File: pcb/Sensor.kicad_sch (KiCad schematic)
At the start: 38 parts, among them IC2 74HC14D-Q100,118, U5 OPA2376xxD

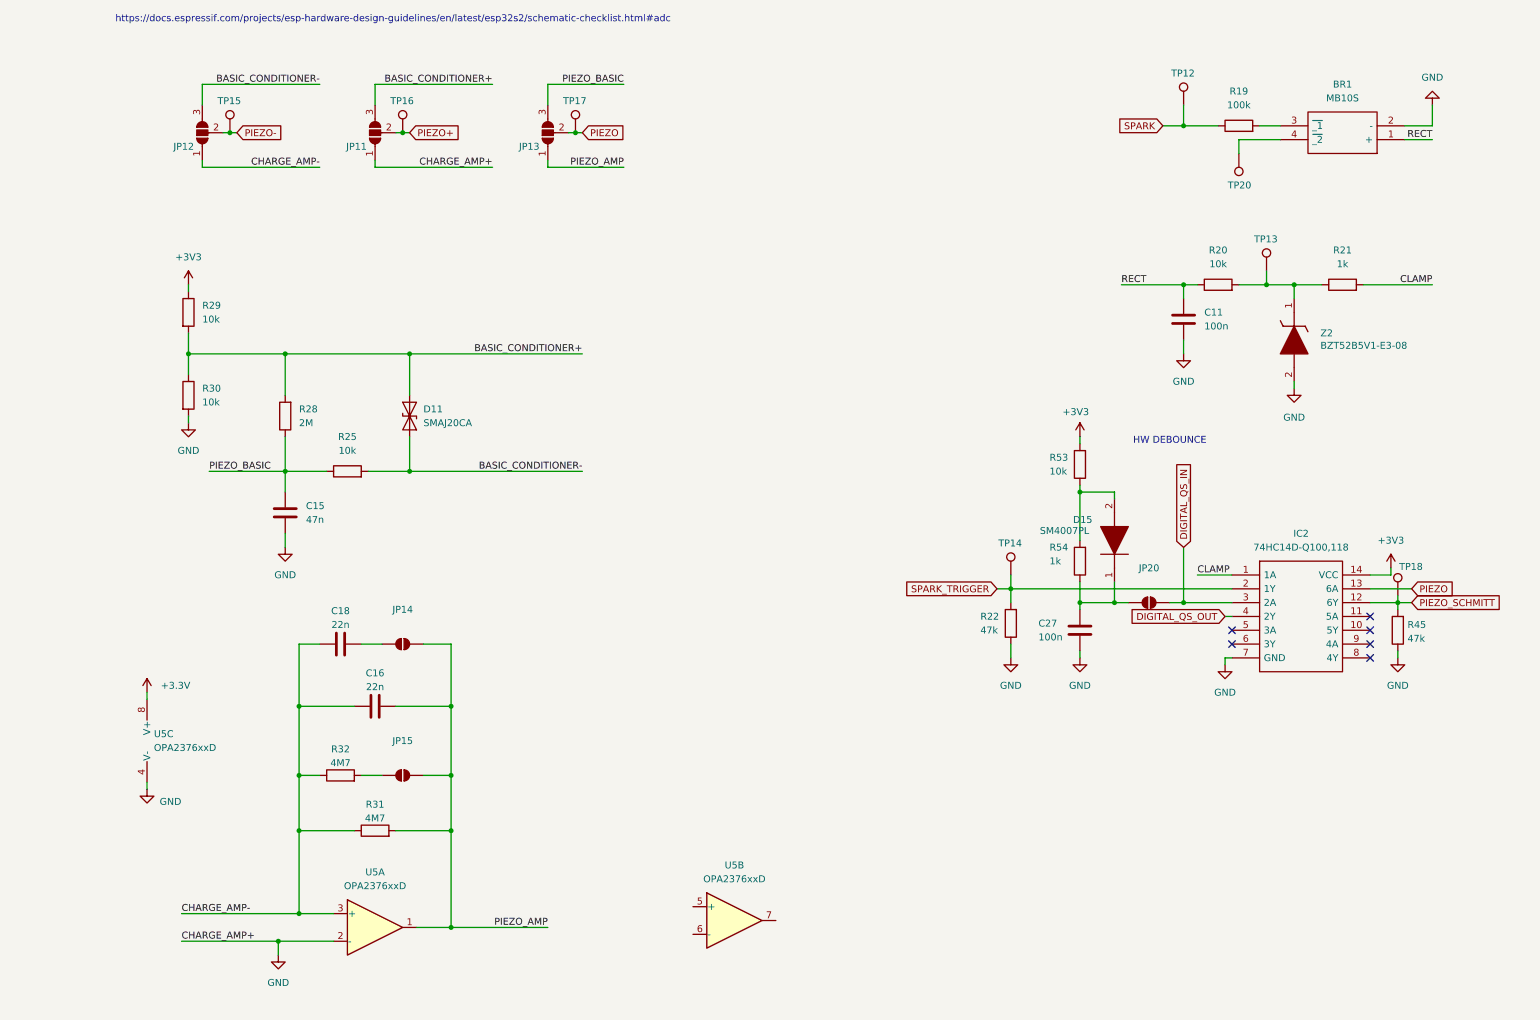
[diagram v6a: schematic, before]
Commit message: enhanced spark detection circuit
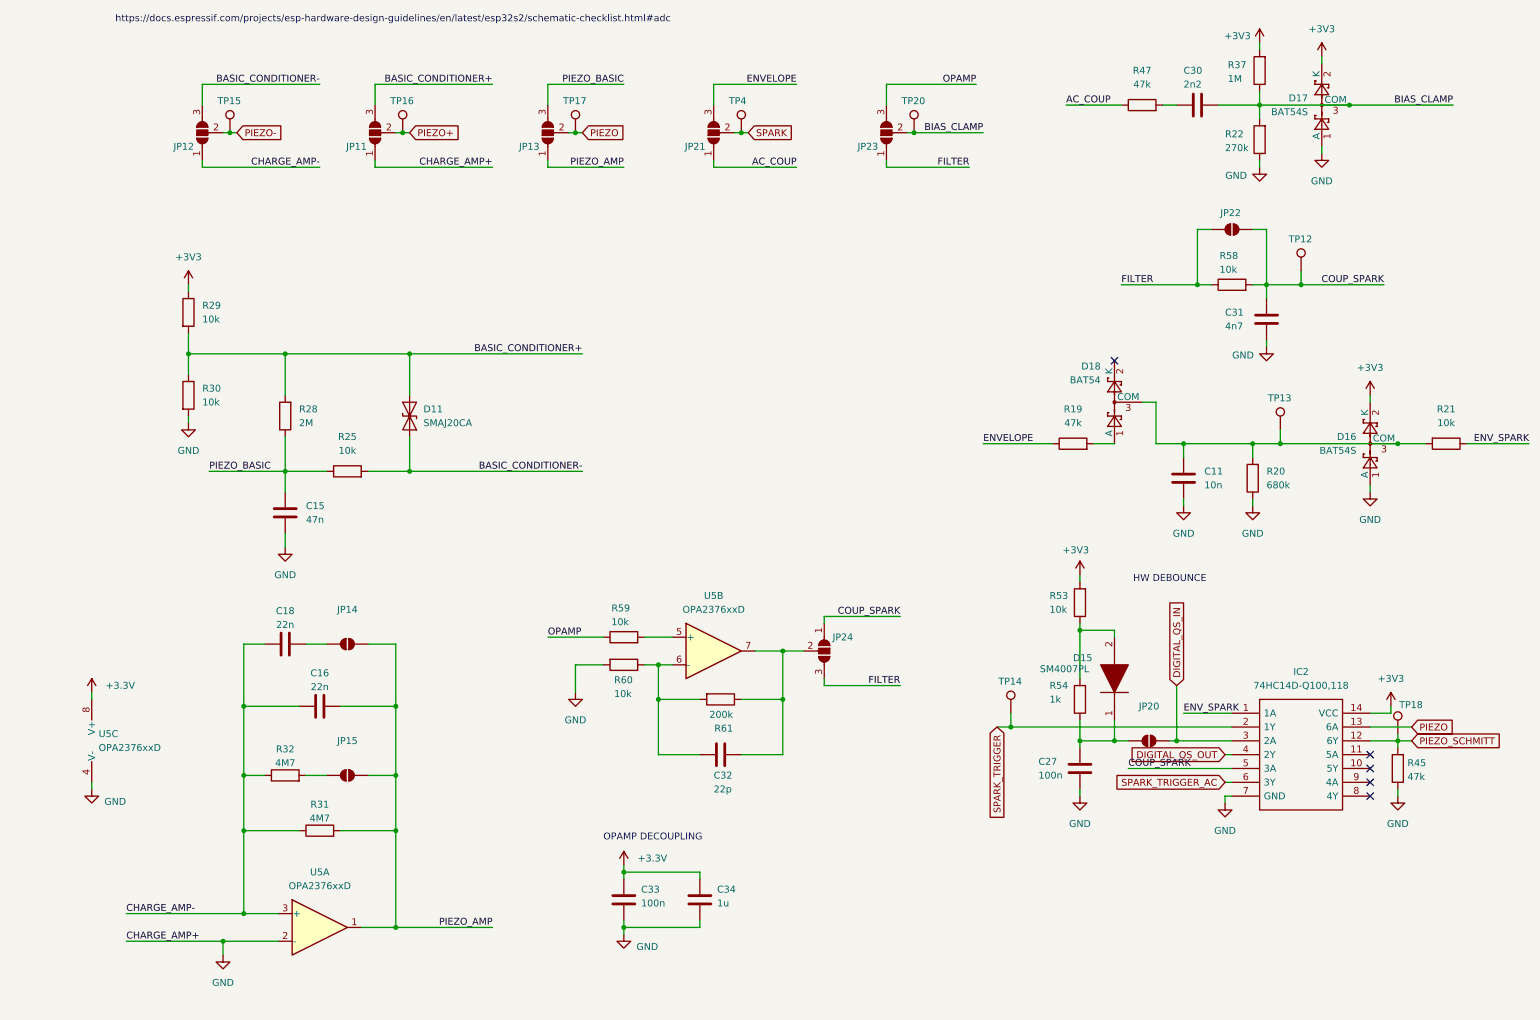
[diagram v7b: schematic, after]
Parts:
- removed BR1: MB10S, SamacSys_Parts:SOP245P670X290-4N, symbol SamacSys_Parts:MB10S
- removed Z2: BZT52B5V1-E3-08, SamacSys_Parts:BZT52B5V1E308, symbol SamacSys_Parts:BZT52B5V1-E3-08
- added C30: 2n2, Capacitor_SMD:C_0603_1608Metric, symbol Device:C
- added C31: 4n7, Capacitor_SMD:C_0603_1608Metric, symbol Device:C
- added C32: 22p, Capacitor_SMD:C_0603_1608Metric, symbol Device:C
- added C33: 100n, Capacitor_SMD:C_0603_1608Metric, symbol Device:C
- added C34: 1u, Capacitor_SMD:C_0603_1608Metric, symbol Device:C
- added D16, D17: BAT54S, Package_TO_SOT_SMD:SOT-23, symbol Diode:BAT54S
- added D18: BAT54, Package_TO_SOT_SMD:SOT-23, symbol Diode:BAT54S
- added JP21, JP23, JP24: SolderJumper_3_Open, Jumper:SolderJumper-3_P1.3mm_Open_RoundedPad1.0x1.5mm, symbol Jumper:SolderJumper_3_Open
- added JP22: SolderJumper_2_Open, Jumper:SolderJumper-2_P1.3mm_Open_RoundedPad1.0x1.5mm, symbol Jumper:SolderJumper_2_Open
- added R37: 1M, Resistor_SMD:R_0603_1608Metric, symbol Device:R
- added R47: 47k, Resistor_THT:R_Axial_DIN0204_L3.6mm_D1.6mm_P1.90mm_Vertical, symbol Device:R
- added R58, R59, R60: 10k, Resistor_SMD:R_0603_1608Metric, symbol Device:R
- added R61: 200k, Resistor_SMD:R_0603_1608Metric, symbol Device:R
- added TP4: TestPoint, Connector_PinHeader_1.00mm:PinHeader_1x01_P1.00mm_Vertical, symbol Connector:TestPoint
- C11: value 100n -> 10n
- R19: value 100k -> 47k
- R20: value 10k -> 680k
- R21: value 1k -> 10k; footprint Resistor_SMD:R_0603_1608Metric -> Resistor_THT:R_Axial_DIN0204_L3.6mm_D1.6mm_P1.90mm_Vertical
- R22: value 47k -> 270k
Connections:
- net +3.3V: now also C33.1, C34.1
- net +3V3: now also D16.2 (K), D17.2 (K), R37.2
- net GND: now also R20.1, C31.1, C33.2, C34.2, D16.1 (A), D17.1 (A), R60.2
- net SPARK: now also JP21.2 (C), TP4.1; no longer R19.1, TP12.1
- net SPARK_TRIGGER: no longer R22.2
- net at R20.2, TP13.1: now also C11.1, R21.2, D16.3 (COM), D18.3 (COM); no longer R21.1
- net BIAS_CLAMP: now reaches TP20.1
- net BIAS_CLAMP: now also R22.2, C30.2, D17.3 (COM), JP23.2 (C), R37.1
- net at R19.2: now also D18.1 (A)
- net COUP_SPARK: now reaches IC2.5 (3A)
- net COUP_SPARK: now also TP12.1, C31.2, JP22.1 (A), JP24.1 (A), R58.2
- net SPARK_TRIGGER_AC: now reaches IC2.6 (3Y)
- net at U5.5 (+): now also R59.2
- net at U5.6 (-): now also C32.2, R60.1, R61.2
- net at U5.7: now also C32.1, JP24.2 (C), R61.1
- net CLAMP renamed ENV_SPARK
- net ENV_SPARK: now also R21.1; no longer R21.2
- removed net RECT: C11.1, R20.1
- new net: C30.1, R47.2
- new net AC_COUP: JP21.1 (A), R47.1
- new net ENVELOPE: JP21.3 (B), R19.1
- new net FILTER: JP22.2 (B), JP23.1 (A), JP24.3 (B), R58.1
- new net OPAMP: JP23.3 (B), R59.1
- no-connect marks 6 -> 5
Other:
- note added: "OPAMP DECOUPLING"
- moved on the sheet: C11, C16, C18, C27, D15, IC2, JP14, JP15, JP20, R19, R20, R31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

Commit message: improved opamp charge amplifier
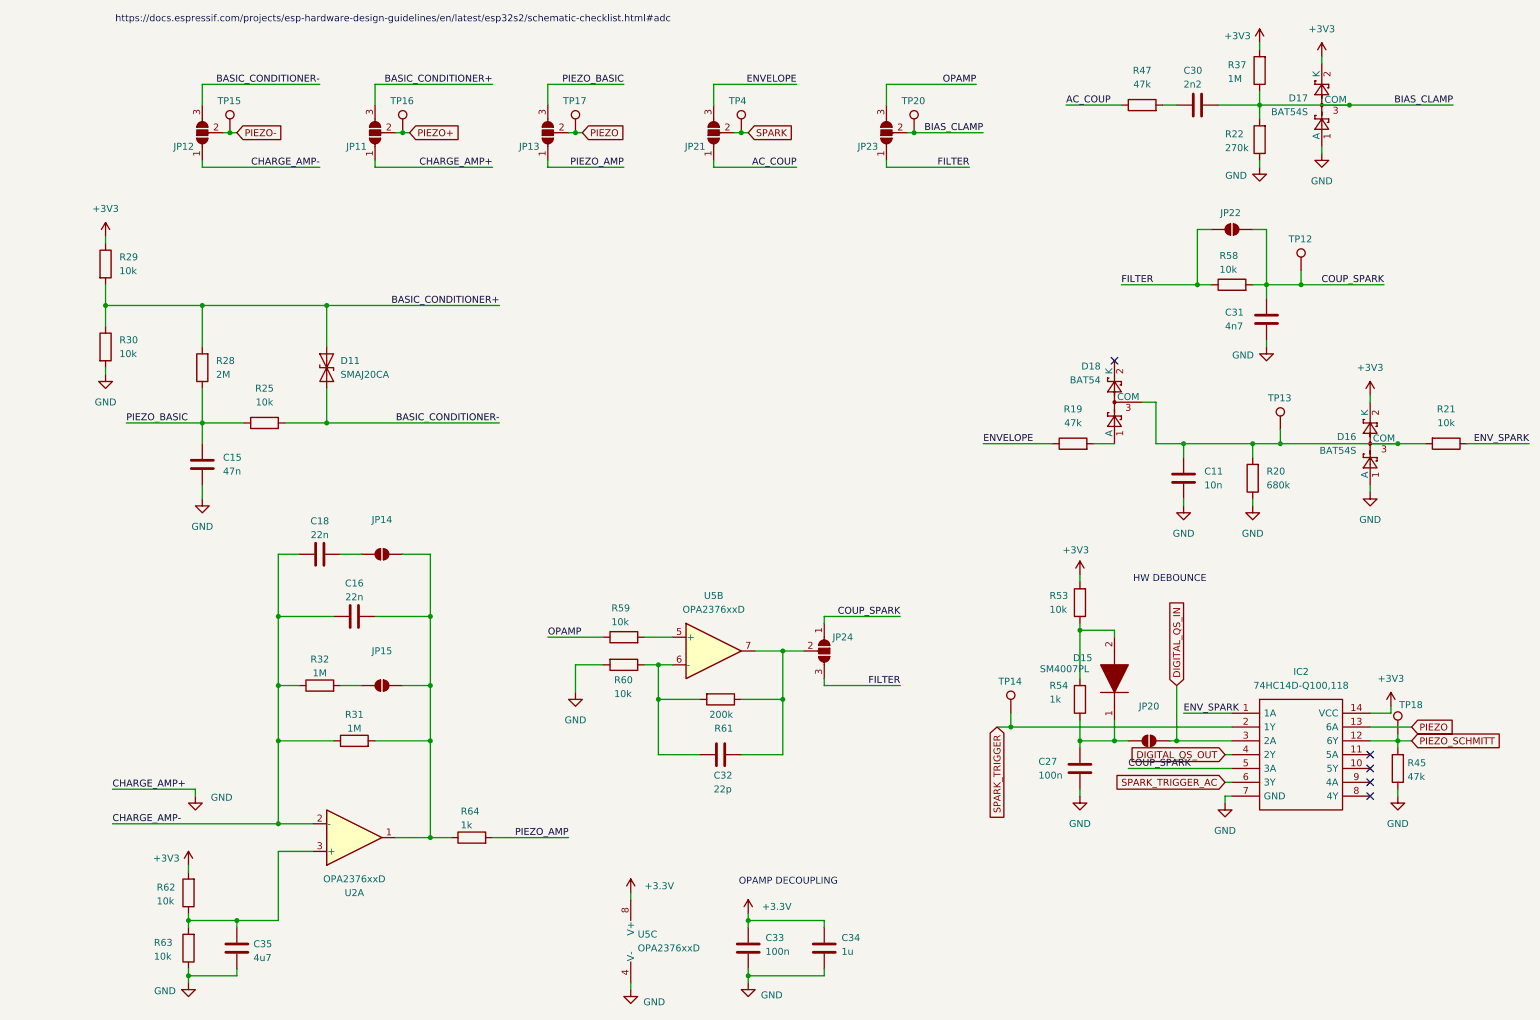
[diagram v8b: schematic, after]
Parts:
- removed unit 1 of U5
- added C35: 4u7, Capacitor_SMD:C_0603_1608Metric, symbol Device:C
- added R62, R63: 10k, Resistor_SMD:R_0603_1608Metric, symbol Device:R
- added R64: 1k, Resistor_SMD:R_0603_1608Metric, symbol Device:R
- added U2: OPA2376xxD, SamacSys_Parts:SOIC127P600X175-8N, symbol Amplifier_Operational:OPA2376xxD
- R31, R32: value 4M7 -> 1M
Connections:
- net +3V3: now also R62.2
- net CHARGE_AMP-: now also U2.2 (-)
- net GND: now also C35.2, R63.1
- net PIEZO_AMP: now also R64.2; no longer C16.2, JP14.1 (A), JP15.1 (A), R31.2
- new net: C16.2, JP14.1 (A), JP15.1 (A), R31.2, R64.1, U2.1
- new net: C35.1, R62.1, R63.2, U2.3 (+)
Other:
- moved on the sheet: C15, C16, C18, C33, C34, D11, JP14, JP15, R25, R28, R29, R30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
